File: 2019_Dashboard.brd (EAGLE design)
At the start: 104.1 x 65.7 mm, 54 parts, among them IC1 MCP23017SO, IC2 MCP23017SO, IC3 MCP23017SO, Y1 16MHz

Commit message: Yeet a few pins
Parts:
- removed IC2: MCP23017SO, adafruit:SO28W
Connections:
- removed net N$16: IC2.22, U$1.6
- removed net N$17: IC2.23, U$1.4
- removed net N$18: IC2.24, U$1.2
- removed net N$19: IC2.25, U$1.1
- removed net N$20: IC2.26, U$1.9
- removed net N$21: IC2.27, U$1.10
- net GND: now also CONTROL.21; no longer IC2.10, IC2.16, IC2.17, U$1.8
- net LAUNCH: now also CONTROL.9; no longer IC2.4
- net LPADDLE: now also CONTROL.24; no longer IC2.1
- net N$1: no longer IC2.12
- net N$10: now also U$1.5
- net N$15: now also IC1.5, U$1.8; no longer IC2.21, U$1.7
- net N$2: no longer IC2.13
- net N$3: now also U$1.7
- net N$4: now also U$1.6
- net N$5: now also U$1.4
- net N$6: now also U$1.2
- net N$7: now also U$1.1
- net N$8: now also U$1.9
- net N$9: now also U$1.10
- net PARTY1: now also CONTROL.10; no longer IC2.5
- net PARTY2: now also CONTROL.11; no longer IC2.6
- net RPADDLE: now also CONTROL.25; no longer IC2.2
- net T/S-TOOGLE: now also CONTROL.26; no longer IC2.3
- net VCC: no longer IC2.15, IC2.18, IC2.9

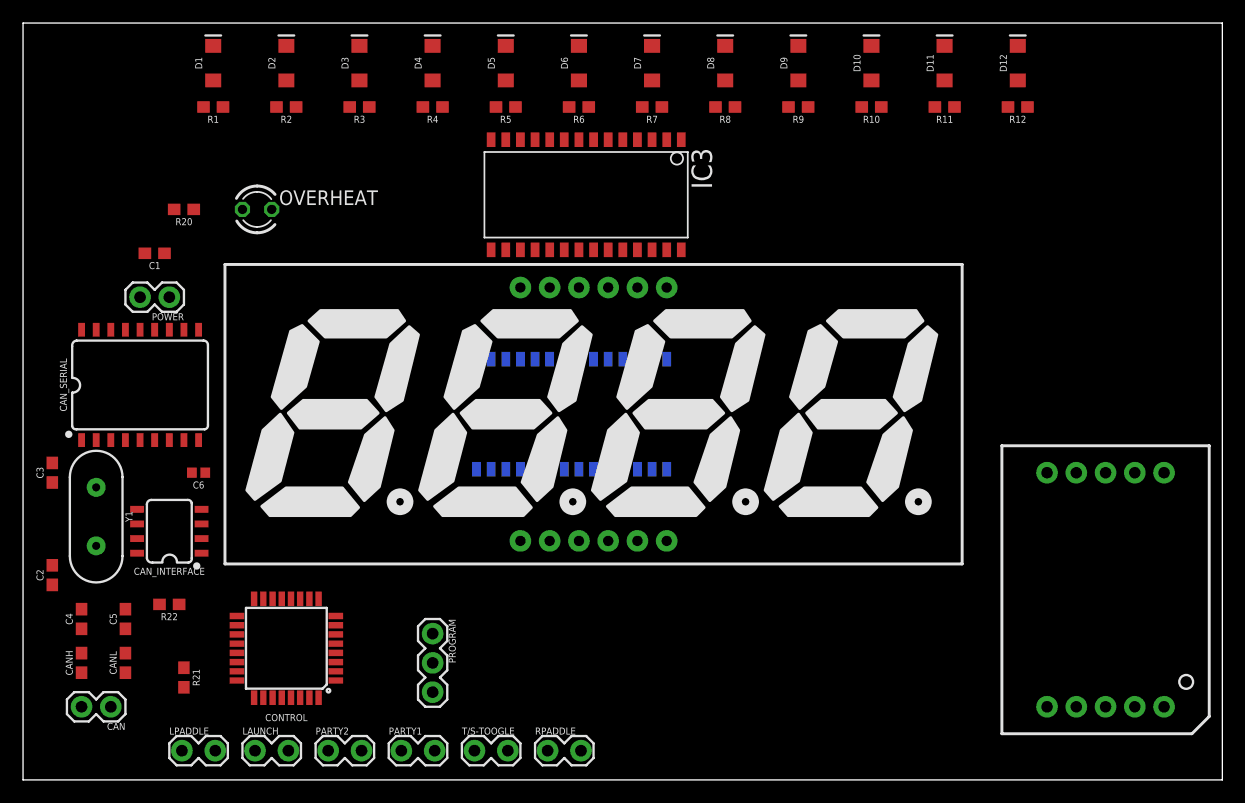
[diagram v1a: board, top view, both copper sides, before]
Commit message: Add files via upload
changed LEDs to Through-hole
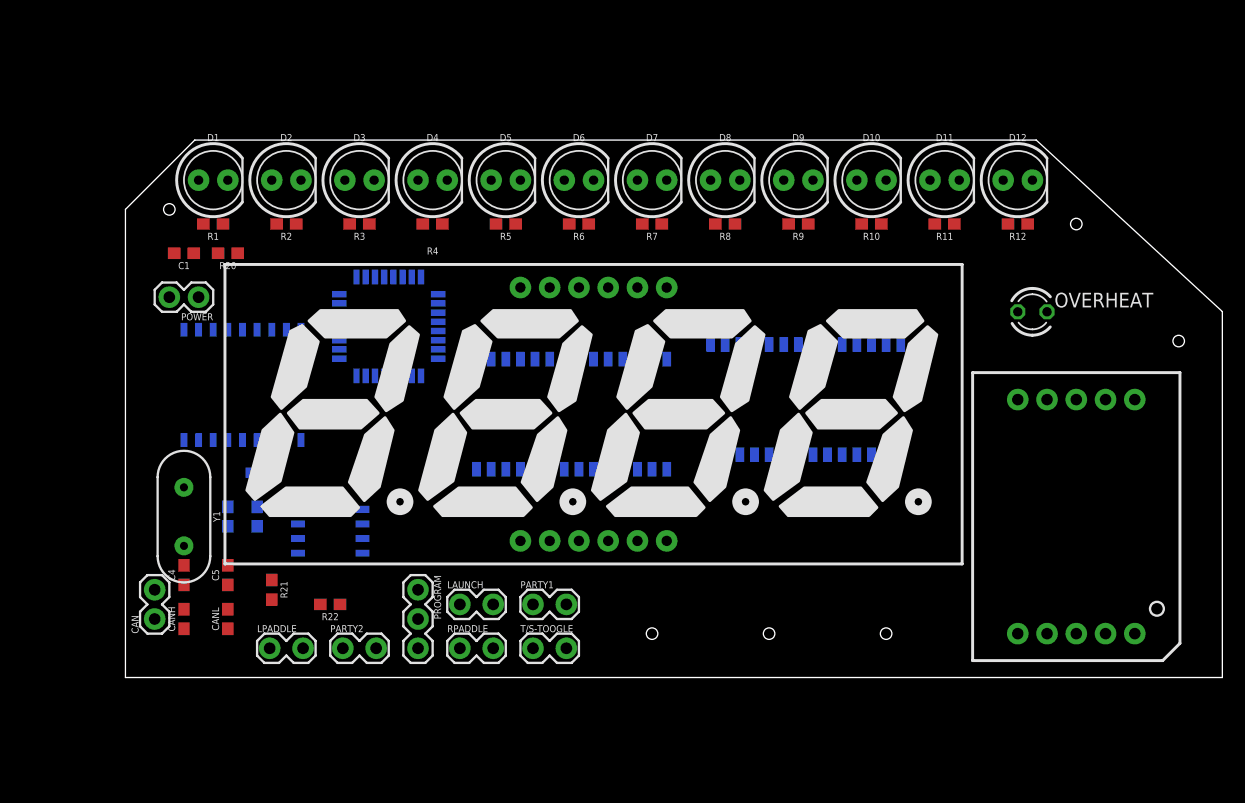
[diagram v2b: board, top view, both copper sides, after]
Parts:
- D1, D2, D3, D4: value RED -> (none); device SparkFun-LED:LED-1206 -> SparkFun-LED:LED_5MM
- D10, D11, D12, D9: value BLUE -> (none); device SparkFun-LED:LED-1206 -> SparkFun-LED:LED_5MM
- D5, D6, D7, D8: value GREEN -> (none); device SparkFun-LED:LED-1206 -> SparkFun-LED:LED_5MM
- moved OVERHEAT 67.9 mm to (125.7, 62.2)
- moved CONTROL 29.3 mm to (69.8, 61.0), flipped to the bottom
- moved IC3 25.1 mm to (105.4, 54.6), flipped to the bottom
- moved LAUNCH 21.8 mm to (76.2, 36.8)
- moved C3 18.2 mm to (58.4, 44.5), flipped to the bottom
- moved PARTY1 17.1 mm to (82.5, 36.8)
- moved C2 16.1 mm to (55.9, 44.5), flipped to the bottom
- moved CAN_INTERFACE 14.0 mm to (64.8, 43.2), flipped to the bottom
- moved R22 14.0 mm to (64.8, 36.8)
- moved LPADDLE 11.7 mm to (59.7, 33.0)
- moved RPADDLE 11.7 mm to (76.2, 33.0)
- moved R21 10.8 mm to (59.7, 38.1)
- moved T/S-TOOGLE 10.2 mm to (82.5, 33.0)
- moved R1 10.2 mm to (54.6, 69.8)
- moved R10 10.2 mm to (111.8, 69.8)
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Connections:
- net GND: now also D1.K, D10.K, D11.K, D12.K, D2.K, D3.K, D4.K, D5.K, D6.K, D7.K, D8.K, D9.K; no longer D1.C, D10.C, D11.C, D12.C, D2.C, D3.C, D4.C, D5.C, D6.C, D7.C, D8.C, D9.C
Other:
- board size 104.1 x 65.7 mm -> 95.2 x 46.7 mm
